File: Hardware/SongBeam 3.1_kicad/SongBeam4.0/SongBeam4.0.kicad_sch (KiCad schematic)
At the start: 128 parts, among them IC3 TPS62842DGRR, IC8 BQ25185, J1 Conn_01x02, J2 Conn_01x04, J3 RJ45, J4 RJ45, Q1 CPH6350-TL-W, Q2 AO6604, U1 PCMD3180IRTWR, U10 LP5907MFX-1.8_NOPB, U11 TPL5110, U13 Teensy4.1, U14 3034, U2 IM66D132H, U3 IM66D132H, U4 IM66D132H, U5 IM66D132H, U6 IM66D132H, U7 IM66D132H, U8 IM66D132H, U9 IM66D132H, X3 USBC

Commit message: tweaks in daugtherboard and develop in the main 4.0 board
changed voltage, added voltage translators and swiched from ethernet to HDMI
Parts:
- removed J3, J4: RJ45, Connector_RJ:RJ45_Molex_9346520x_Horizontal, symbol Connector:RJ45
- added C35, C36: 0.1uF, Capacitor_SMD:C_0805_2012Metric, symbol Device:C_Small
- added J5: HDMI_A, symbol Connector:HDMI_A
- added R36: 10K, Resistor_SMD:R_0805_2012Metric, symbol Device:R_Small
- added R37, R38, R42, R43, R44: 100K, Resistor_SMD:R_0805_2012Metric, symbol Device:R_Small
- added U12: TXS0108EPW, Package_SO:TSSOP-20_4.4x6.5mm_P0.65mm, symbol Logic_LevelTranslator:TXS0108EPW
- C1: value 10uF -> 1uF
- C10: value 1uF -> 10uF
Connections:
- net micgrp_1IN is gone; now on net micgrp_1IN_1.8V: U6.4 (CLK), U7.4 (CLK)
- net +1V8: now also C10.2, C9.1, U1.19 (IOVDD), C35.1, R36.1, U12.10 (OE), U12.2 (VCCA); no longer C1.1, C2.2, U1.1 (AVDD)
- net +3.3V: now also C1.1, C2.2, U1.1 (AVDD), C36.1, J5.18 (+5V), U12.19 (VCCB); no longer C10.2, C9.1, U1.19 (IOVDD)
- net GND: now also C35.2, C36.2, J5.11 (CKS), J5.17 (GND), J5.2 (D2S), J5.5 (D1S), J5.8 (D0S), R36.2, U12.11 (GND)
- net MCLK_TDM1_1.8V: now reaches U1.20 (GPIO1)
- net MCLK_TDM1_1.8V: now also U12.4 (A3)
- net BCLK renamed BCLK_TDM1_1.8V
- net BCLK_TDM1_1.8V: now also U12.1 (A1)
- net FSYNC renamed FSYNC_1.8V
- net FSYNC_1.8V: now also U12.3 (A2)
- net SCL_MOSI renamed SCL_MOSI_1.8V
- net SCL_MOSI_1.8V: now also U12.8 (A7)
- net SDA_SSZ renamed SDA_SSZ_1.8V
- net SDA_SSZ_1.8V: now also U12.7 (A6)
- net SHDNZ renamed SHDNZ_1.8V
- net SHDNZ_1.8V: now also R38.1
- net TDM_OUT renamed OUTPUT_TDM1_1.8V
- net OUTPUT_TDM1_1.8V: now also U12.6 (A5)
- net micGRP_1IN renamed micgrp_1IN_1.8V
- net micGRP_2IN renamed micGRP_2IN_1.8V
- net micGRP_2out renamed micGRP_2out_1.8V
- net micGRP_3IN renamed micGRP_3IN_1.8V
- net micGRP_3out renamed micGRP_3out_1.8V
- net micGRP_4IN renamed micGRP_4IN_1.8V
- net micGRP_4out renamed micGRP_4out_1.8V
- new net: R38.2, U12.9 (A8)
- new net BCLK_TDM1_3.3V: J5.1 (D2+), U12.20 (B1)
- new net FSYNC_3.3V: J5.10 (CK+), U12.18 (B2)
- new net MCLK_TDM1_3.3V: J5.4 (D1+), U12.17 (B3)
- new net OUTPUT_TDM1_3.3V: J5.7 (D0+), U12.15 (B5)
- new net SCL_MOSI_3.3V: J5.15 (SCL), U12.13 (B7)
- new net SDA_SSZ_3.3V: J5.13 (CEC), U12.14 (B6)
- new net SHDNZ_3.3V: J5.14 (UTILITY), U12.12 (B8)
- no-connect marks 25 -> 32
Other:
- note added: "1.8V to 3.3V clock and data converter"
- note added: "Conection ports"
- note added: "Daughter board connection"
- note added: "TO DO: implement ADAFRUIT change every resistor and capacitor number add every part into the libraries fix lighting"
- note added: "Voltage translators"
- note added: "daisy-chaining ->"
- note added: "mic data testing port"
- note removed: "Conection port"
- moved on the sheet: C27, C28, C29, C30, C31, C32, C33, C34, CHG0, D2, F1, FAULT0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

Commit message: Small tweaks, implementing the power modules
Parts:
- removed C29: 22uF, Adafruit bq25185 Breakout:0805-NO, symbol Adafruit bq25185 Breakout-eagle-import:CAP_CERAMIC0805-NOOUTLINE
- removed D2: MBRX120, Adafruit bq25185 Breakout:SOD-123FL, symbol Adafruit bq25185 Breakout-eagle-import:DIODE-SCHOTTKYSOD-123FL
- removed JP2: HEADER-1X6OVALWAVE, Adafruit bq25185 Breakout:1X06_OVALWAVE, symbol Adafruit bq25185 Breakout-eagle-import:HEADER-1X6OVALWAVE
- removed R19, R21: 5.1K, Adafruit bq25185 Breakout:0603-NO, symbol Adafruit bq25185 Breakout-eagle-import:RESISTOR_0603_NOOUT
- removed unit 1 of VBAT0
- removed X3: USBC, Adafruit bq25185 Breakout:USB_C_CUSB31-CFM2AX-01-X, symbol Adafruit bq25185 Breakout-eagle-import:USB_C
- added C29: 1uF, Capacitor_SMD:C_0805_2012Metric, symbol Device:C_Small
- added C37: 22uF, Adafruit bq25185 Breakout:0805-NO, symbol Adafruit bq25185 Breakout-eagle-import:CAP_CERAMIC0805-NOOUTLINE
- added C38, C40, C41: 22uF, Capacitor_SMD:C_0805_2012Metric, symbol Device:C_Small
- added CHG1: ORANGE, Adafruit bq25185 Breakout:CHIPLED_0805_NOOUTLINE, symbol Adafruit bq25185 Breakout-eagle-import:LED0805_NOOUTLINE
- added D1, D4: MBRX120, Adafruit bq25185 Breakout:SOD-123FL, symbol Adafruit bq25185 Breakout-eagle-import:DIODE-SCHOTTKYSOD-123FL
- added FAULT1: RED, Adafruit bq25185 Breakout:CHIPLED_0805_NOOUTLINE, symbol Adafruit bq25185 Breakout-eagle-import:LED0805_NOOUTLINE
- added J3, J6: USB_B_Micro, symbol Connector:USB_B_Micro
- added J4: Conn_01x09, symbol Connector_Generic:Conn_01x09
- added J7: Conn_01x02_Socket (JST 2 pin), symbol Connector:Conn_01x02_Socket
- added JP3: HEADER-1X6OVALWAVE, Adafruit bq25185 Breakout:1X06_OVALWAVE, symbol Adafruit bq25185 Breakout-eagle-import:HEADER-1X6OVALWAVE
- added R45: 10000K, Resistor_SMD:R_0805_2012Metric, symbol Device:R_Small
- added R46: 2.2K, Resistor_SMD:R_0805_2012Metric, symbol Device:R_Small
- added R47, R48, R49, R50, R51: 33R, Resistor_SMD:R_0805_2012Metric, symbol Device:R_Small
- added R52: 10K, Adafruit bq25185 Breakout:0603-NO, symbol Adafruit bq25185 Breakout-eagle-import:RESISTOR_0603_NOOUT
- added R53, R54: 1K, Adafruit bq25185 Breakout:0603-NO, symbol Adafruit bq25185 Breakout-eagle-import:RESISTOR_0603_NOOUT
- added R56: 300, Adafruit bq25185 Breakout:0603-NO, symbol Adafruit bq25185 Breakout-eagle-import:RESISTOR_0603_NOOUT
- added R59: 5.1K, Adafruit bq25185 Breakout:0603-NO, symbol Adafruit bq25185 Breakout-eagle-import:RESISTOR_0603_NOOUT
- added R60: 6.8K, Adafruit bq25185 Breakout:0603-NO, symbol Adafruit bq25185 Breakout-eagle-import:RESISTOR_0603_NOOUT
- added SW1: SW_SPDT, symbol Switch:SW_SPDT
- added U15: BQ25185DLHR, WSON10_DLH_TEX, symbol BQ25185DLHR:BQ25185DLHR
- R37, R42, R44: value 100K -> 33R
- R43: value 100K -> 2.2K
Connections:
- net BCLK_TDM1 is gone; now on an unnamed net: U13.21 (29_TX7)
- net INPUT_TDM1 is gone; now on an unnamed net: U13.8 (6_OUT1D)
- net MCLK_TDM1 is gone; now on an unnamed net: U13.23 (31_CTX3)
- net 5.0V: now also JP3.4
- net BCLK_TDM1_3.3V: now also R44.1, J4.9 (Pin_9); no longer J5.1 (D2+)
- net FSYNC_1.8V: no longer U12.3 (A2)
- net GND: now also C29.1, C37.2, C38.2, C40.2, C41.1, J3.5 (GND), J3.6 (Shield), J4.1 (Pin_1), J6.5 (GND), J6.6 (Shield), J7.1 (Pin_1), JP3.1, JP3.3, JP3.5, R52.1, R56.2, R59.2, R60.2, U15.5 (GND); no longer C21.1, C22.1, R10.2, R11.2, R12.2, R13.1, U1.6 (PDMDIN1_GPI1)
- net MCLK_TDM1_3.3V: now also R42.1, J4.8 (Pin_8); no longer J5.4 (D1+)
- net OUTPUT_TDM1_3.3V: now also R37.1, J4.7 (Pin_7); no longer J5.7 (D0+)
- net SCL_MOSI_3.3V: now also R43.1, U13.41 (19_A5_SCL), J4.4 (Pin_4)
- net SDA_SSZ_3.3V: now also U13.40 (18_A4_SDA), J4.5 (Pin_5), R46.2
- net SHDNZ_3.3V: now also U13.39 (17_A3_TX4_SDA1), J4.3 (Pin_3), R45.1
- net VBAT: now also C41.2, J7.2 (Pin_2), JP3.6, U15.2 (BAT)
- net VBUS: now also C29.2, C37.1, C38.1, D1.C, D4.C, U15.10 (IN)
- net god knows 1: now reaches J1.1 (Pin_1), JP1.2 (B)
- net god knows 3: now reaches Q2.1 (G1), R18.1
- net Done: now reaches U13.24 (32_OUT1B)
- net Done: now also R35.1, U11.4 (DONE), J4.2 (Pin_2)
- net at D3.1, U13.46 (3V3): now also R43.2, R45.2, R46.1
- net at D2.A: now also JP3.2
- net battery voltage: now reaches R18.2, R20.1
- net BCLK_TDM2: no longer names the net of U13.4 (2_OUT2)
- net BCLK_TDM2: now also R50.2
- net FSYNC_3.3V renamed FSYNC_TDM1_3.3V
- net FSYNC_TDM1_3.3V: now also J4.6 (Pin_6), R47.1; no longer J5.10 (CK+)
- net INPUT_TDM2: no longer names the net of U13.5 (3_LRCLK2)
- net INPUT_TDM2: now also R49.2
- net MCLK_TDM2: no longer names the net of U13.33 (41_A17)
- net MCLK_TDM2: now also R48.1
- net OUTPUT_TDM1: no longer names the net of U13.20 (28_RX7)
- net OUTPUT_TDM1: now also R47.2
- net OUTPUT_TDM2: no longer names the net of U13.3 (1_TX1_CTX2_MISO1)
- net OUTPUT_TDM2: now also R51.2
- new net: R53.1, U15.3 (STAT2)
- new net: CHG1.C, R53.2
- new net: R56.1, U15.8 (ISET)
- new net: R52.2, U15.4 (/CE)
- new net: SW1.2 (B), U15.7 (ILIM/VSET)
- new net: R54.1, U15.9 (STAT1)
- new net: R59.1, SW1.1 (A)
- new net: D1.A, J3.1 (VBUS)
- new net: D4.A, J6.1 (VBUS)
- new net: FAULT1.C, R54.2
- new net: R60.1, SW1.3 (C)
- new net +5V: C40.1, CHG1.A, FAULT1.A, U15.1 (SYS)
- new net BCLK_TDM2_3.3V: J5.1 (D2+), R50.1
- new net FSYNC_TDM1_1.8V: U12.3 (A2)
- new net FSYNC_TDM2_3.3V: J5.10 (CK+), R51.1
- new net MCLK_TDM2_3.3V: J5.4 (D1+), R48.2
- new net OUTPUT_TDM2_3.3V: J5.7 (D0+), R49.1
- new net micGRP_1out_1.8V: C21.1, C22.1, R10.2, R11.2, R12.2, R13.1, U1.6 (PDMDIN1_GPI1)
- no-connect marks 32 -> 38
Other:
- note added: "300Ω = 1000mA"
- note added: "5.1KΩ = 3.65V / 1A 6.8KΩ = 4.05V / 1A"
- note added: "ADD CAPACITOR FOR MAINTAINING THE BOARD ON"
- note added: "Energy distribution, debugging and intake"
- note added: "ON LED, MAYBE WE DO NOT NEED IT"
- note added: "PCMD3180 and timer testing port"
- note added: "THIS NEED TO BE CONECTED TO THE ADAFRUIT SOLAR MODULE IMPLEMENTATION"
- moved on the sheet: C10, C30, C31, C32, C33, C34, C7, C8, C9, CHG0, D2, D3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

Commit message: small tweaks
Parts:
- removed C30, C31, C37: 22uF, Adafruit bq25185 Breakout:0805-NO, symbol Adafruit bq25185 Breakout-eagle-import:CAP_CERAMIC0805-NOOUTLINE
- removed CHG0: ORANGE, Adafruit bq25185 Breakout:CHIPLED_0805_NOOUTLINE, symbol Adafruit bq25185 Breakout-eagle-import:LED0805_NOOUTLINE
- removed D1: MBRX120, Adafruit bq25185 Breakout:SOD-123FL, symbol Adafruit bq25185 Breakout-eagle-import:DIODE-SCHOTTKYSOD-123FL
- removed FAULT0: RED, Adafruit bq25185 Breakout:CHIPLED_0805_NOOUTLINE, symbol Adafruit bq25185 Breakout-eagle-import:LED0805_NOOUTLINE
- removed IC8: BQ25185, Adafruit bq25185 Breakout:WSON10, symbol Adafruit bq25185 Breakout-eagle-import:BQ25185
- removed J3: USB_B_Micro, symbol Connector:USB_B_Micro
- removed JP2, JP4: FIDUCIAL1.5X3, Adafruit bq25185 Breakout:FIDUCIAL_0.5MM, symbol Adafruit bq25185 Breakout-eagle-import:FIDUCIAL_0.5MM
- removed JP7: HEADER-1X676MIL, Adafruit bq25185 Breakout:1X06_ROUND_76, symbol Adafruit bq25185 Breakout-eagle-import:HEADER-1X676MIL
- removed R23, R24: 1K, Adafruit bq25185 Breakout:0603-NO, symbol Adafruit bq25185 Breakout-eagle-import:RESISTOR_0603_NOOUT
- removed R25, R31: 10K, Adafruit bq25185 Breakout:0603-NO, symbol Adafruit bq25185 Breakout-eagle-import:RESISTOR_0603_NOOUT
- removed R26: 600, Adafruit bq25185 Breakout:0603-NO, symbol Adafruit bq25185 Breakout-eagle-import:RESISTOR_0603_NOOUT
- removed R27: 300, Adafruit bq25185 Breakout:0603-NO, symbol Adafruit bq25185 Breakout-eagle-import:RESISTOR_0603_NOOUT
- removed R28: 13K, Adafruit bq25185 Breakout:0603-NO, symbol Adafruit bq25185 Breakout-eagle-import:RESISTOR_0603_NOOUT
- removed R29: 1200, Adafruit bq25185 Breakout:0603-NO, symbol Adafruit bq25185 Breakout-eagle-import:RESISTOR_0603_NOOUT
- removed R30: 5.1K, Adafruit bq25185 Breakout:0603-NO, symbol Adafruit bq25185 Breakout-eagle-import:RESISTOR_0603_NOOUT
- removed SJ1, SJ2, SJ3: SOLDERJUMPER_CLOSED, Adafruit bq25185 Breakout:SOLDERJUMPER_CLOSEDWIRE, symbol Adafruit bq25185 Breakout-eagle-import:SOLDERJUMPER_CLOSED
- removed SJ4, SJ5, SJ6: SOLDERJUMPER, Adafruit bq25185 Breakout:SOLDERJUMPER_ARROW_NOPASTE, symbol Adafruit bq25185 Breakout-eagle-import:SOLDERJUMPER
- removed U$11, U$16, U$18, U$19: MOUNTINGHOLE2.5, Adafruit bq25185 Breakout:MOUNTINGHOLE_2.5_PLATED, symbol Adafruit bq25185 Breakout-eagle-import:MOUNTINGHOLE2.5
- added R21: 10K, Adafruit bq25185 Breakout:0603-NO, symbol Adafruit bq25185 Breakout-eagle-import:RESISTOR_0603_NOOUT
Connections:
- net GND: now also R21.1
- net at U15.6 (TS/MR): now also R21.2
- no-connect marks 38 -> 35
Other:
- note added: "step down covnerter from 1.8 to any to target voltage"
- note removed: "300Ω = 1000mA 600Ω = 500mA 1200Ω = 250mA"
- note removed: "5.1KΩ = 3.65V / 1A 12KΩ = 4.2V / 1A"
- moved on the sheet: D2, JP3, VBAT0B, VBAT0C, VSYS0A, VSYS0B, VSYS0C

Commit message: tweaks better
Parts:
- removed D2: MBRX120, Adafruit bq25185 Breakout:SOD-123FL, symbol Adafruit bq25185 Breakout-eagle-import:DIODE-SCHOTTKYSOD-123FL
- removed J1: Conn_01x02, Connector_Wire:SolderWire_1x02_P2.52, symbol Connector_Generic:Conn_01x02
- removed J7: Conn_01x02_Socket (JST 2 pin), symbol Connector:Conn_01x02_Socket
- removed JP3: HEADER-1X6OVALWAVE, Adafruit bq25185 Breakout:1X06_OVALWAVE, symbol Adafruit bq25185 Breakout-eagle-import:HEADER-1X6OVALWAVE
- removed R22: 1K, Adafruit bq25185 Breakout:0603-NO, symbol Adafruit bq25185 Breakout-eagle-import:RESISTOR_0603_NOOUT
- removed VBAT0, VSYS0: JST2PH, Adafruit bq25185 Breakout:JSTPH2_BATT, symbol Adafruit bq25185 Breakout-eagle-import:CON_JST_PH_2PIN_MT_BATT
- removed VSYSOK0: GREEN, Adafruit bq25185 Breakout:CHIPLED_0805_NOOUTLINE, symbol Adafruit bq25185 Breakout-eagle-import:LED0805_NOOUTLINE
- added J3: JST2PH CONECTOR, symbol Connector:Conn_01x02_Socket
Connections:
- net god knows 1 is gone; now on net PWR: J1.1 (Pin_1), JP1.2 (B)
- net god knows 3 is gone; now on net emrg_pwr_swch: Q2.1 (G1), R18.1
- net +5V: now also F1.1
- net GND: now also J3.1 (Pin_1)
- net VBAT: now also J3.2 (Pin_2)
- net battery voltage: now also U13.17 (25_A11_RX6_SDA2)
- net emrg_pwr_swch: now reaches U13.11 (9_OUT1C)
- net PWR: now reaches U13.48 (VIN)
- no-connect marks 35 -> 34
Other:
- note added: "ADD DIODE"
- note added: "Battery conector"
- note added: "MAKE ALL CAPACITORSS AND RESITANCE CERAMIC"
- note added: "Solar panel conector"
- note added: "step down covnerter from 1.8 to 5v"
- note removed: "ON LED, MAYBE WE DO NOT NEED IT"
- note removed: "THIS NEED TO BE CONECTED TO THE ADAFRUIT SOLAR MODULE IMPLEMENTATION"
- note removed: "step down covnerter from 1.8 to any to target voltage"
- moved on the sheet: C29, C32, C33, C34, C38, C40, C41, CHG1, D4, F1, FAULT1, IC3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

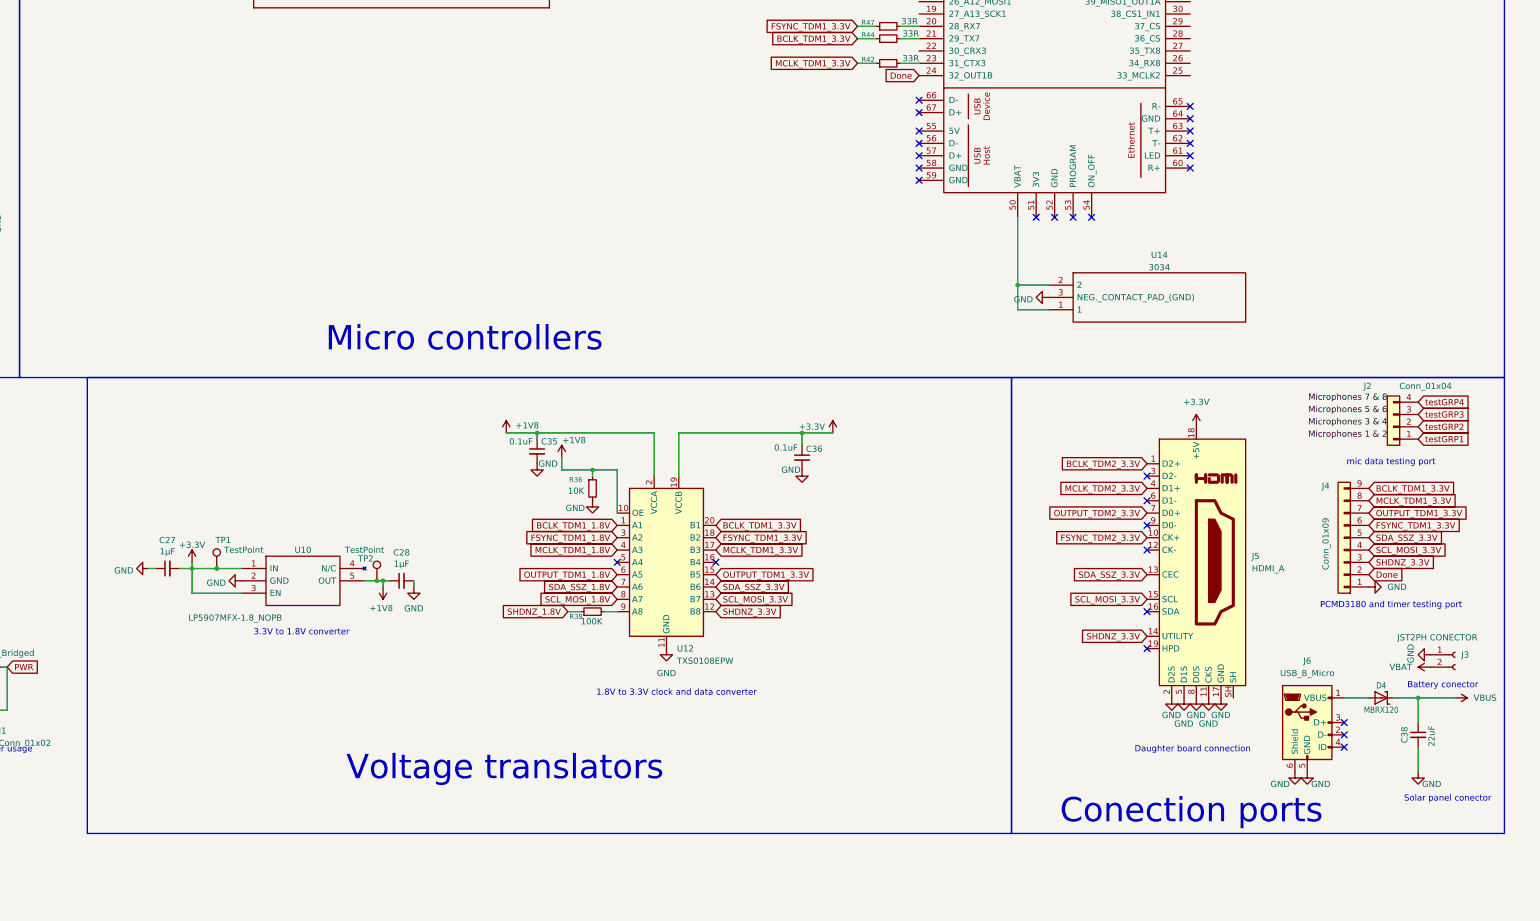
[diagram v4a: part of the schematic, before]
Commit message: backup switch to cat6
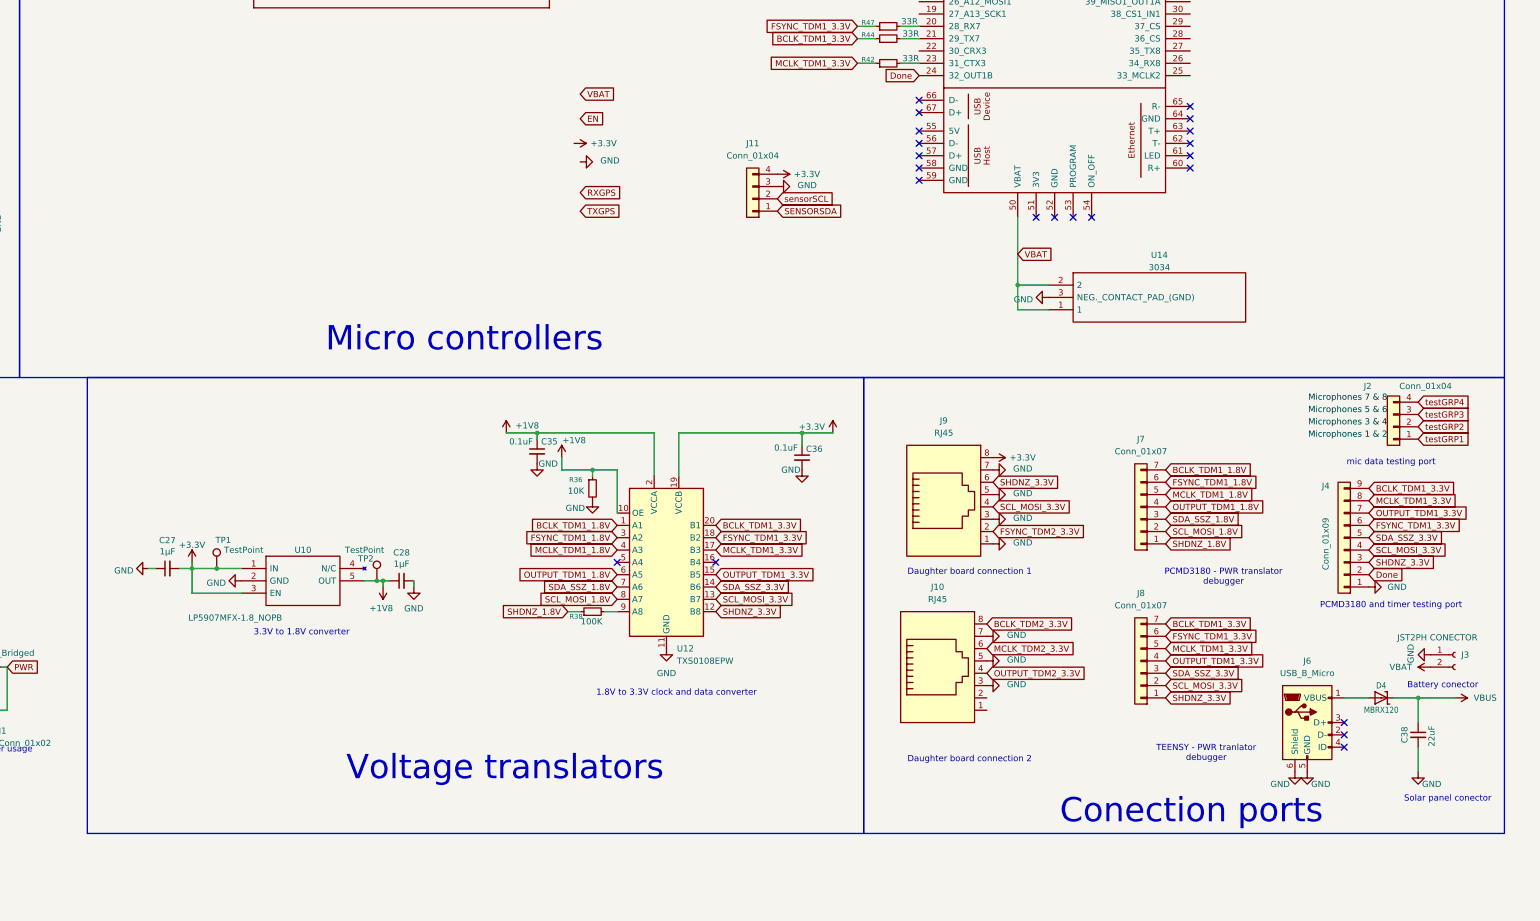
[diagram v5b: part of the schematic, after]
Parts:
- removed J5: HDMI_A, symbol Connector:HDMI_A
- added J10, J9: RJ45, symbol Connector:RJ45
- added J11: Conn_01x04, symbol Connector_Generic:Conn_01x04
- added J7, J8: Conn_01x07, symbol Connector_Generic:Conn_01x07
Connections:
- net +3.3V: now also J11.4 (Pin_4), J9.8
- net BCLK_TDM1_1.8V: now also J7.7 (Pin_7)
- net BCLK_TDM1_3.3V: now also J8.7 (Pin_7)
- net BCLK_TDM2_3.3V: now also J10.8
- net FSYNC_TDM1_1.8V: now also J7.6 (Pin_6)
- net FSYNC_TDM1_3.3V: now also J8.6 (Pin_6)
- net FSYNC_TDM2_3.3V: now also J9.2
- net GND: now also J10.3, J10.5, J10.7, J11.3 (Pin_3), J9.1, J9.3, J9.5, J9.7
- net MCLK_TDM1_1.8V: now also J7.5 (Pin_5)
- net MCLK_TDM1_3.3V: now also J8.5 (Pin_5)
- net MCLK_TDM2_3.3V: now also J10.6
- net OUTPUT_TDM1_1.8V: now also J7.4 (Pin_4)
- net OUTPUT_TDM1_3.3V: now also J8.4 (Pin_4)
- net OUTPUT_TDM2_3.3V: now also J10.4
- net SCL_MOSI_1.8V: now also J7.2 (Pin_2)
- net SCL_MOSI_3.3V: now also J8.2 (Pin_2), J9.4
- net SDA_SSZ_1.8V: now also J7.3 (Pin_3)
- net SDA_SSZ_3.3V: now also J8.3 (Pin_3)
- net SHDNZ_1.8V: now also J7.1 (Pin_1)
- net SHDNZ_3.3V: now also J8.1 (Pin_1), J9.6
- net VBAT: now also U13.50 (VBAT), U14.1, U14.2
- new net SENSORSDA: J11.1 (Pin_1)
- new net sensorSCL: J11.2 (Pin_2)
- no-connect marks 34 -> 28
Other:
- note added: "Daughter board connection 1"
- note added: "Daughter board connection 2"
- note added: "PCMD3180 - PWR translator debugger"
- note added: "TEENSY - PWR tranlator debugger"
- note removed: "Daughter board connection"
